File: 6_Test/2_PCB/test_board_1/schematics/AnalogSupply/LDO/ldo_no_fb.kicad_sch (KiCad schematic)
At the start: 6 parts, among them U1 TPS74501PDRVR

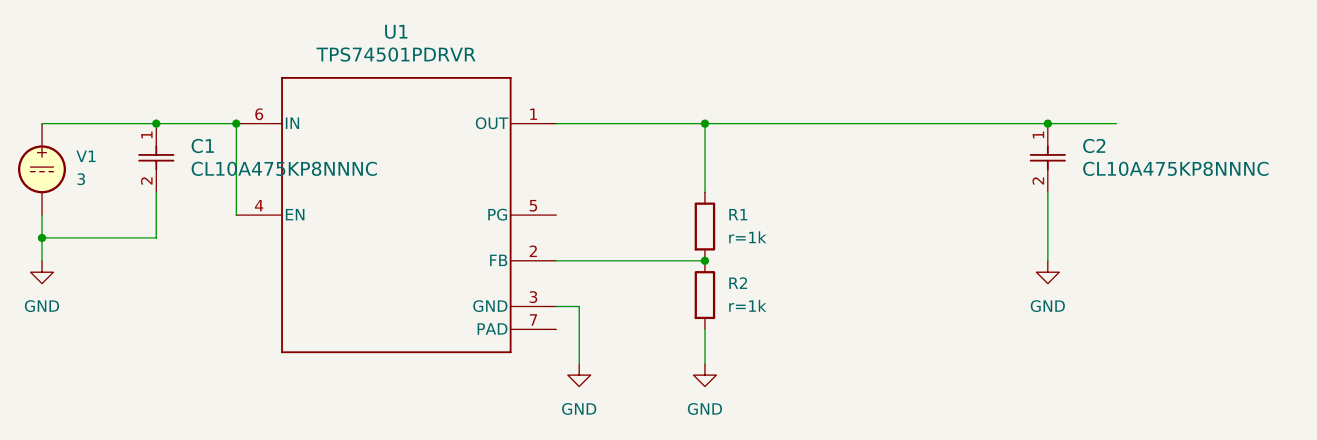
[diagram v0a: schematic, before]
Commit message: ldo simulations done
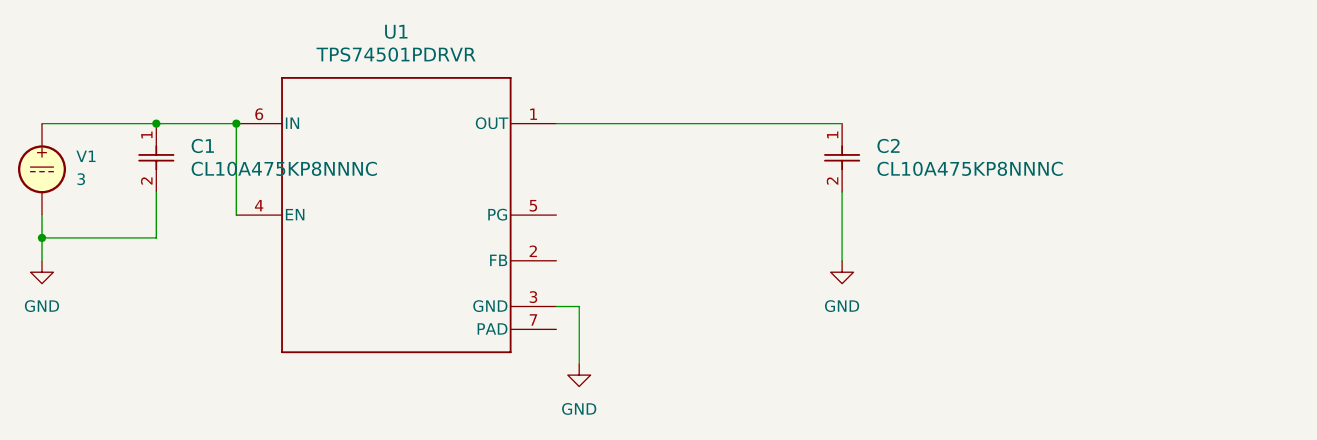
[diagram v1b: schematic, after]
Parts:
- removed R1, R2: ${SIM.PARAMS}, symbol Device:R
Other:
- moved on the sheet: C2
